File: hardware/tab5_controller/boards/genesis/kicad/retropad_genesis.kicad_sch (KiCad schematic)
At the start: 46 parts, among them J1 Tab5 Ext.Port1, J2 SWD, SW1 UP, SW10 START, SW11 MENU, SW12 L, SW13 R, SW2 DOWN, SW3 LEFT, SW4 RIGHT, SW5 X, SW6 B, SW7 Y, SW8 A, SW9 SELECT, U1 STM32F030C8T6

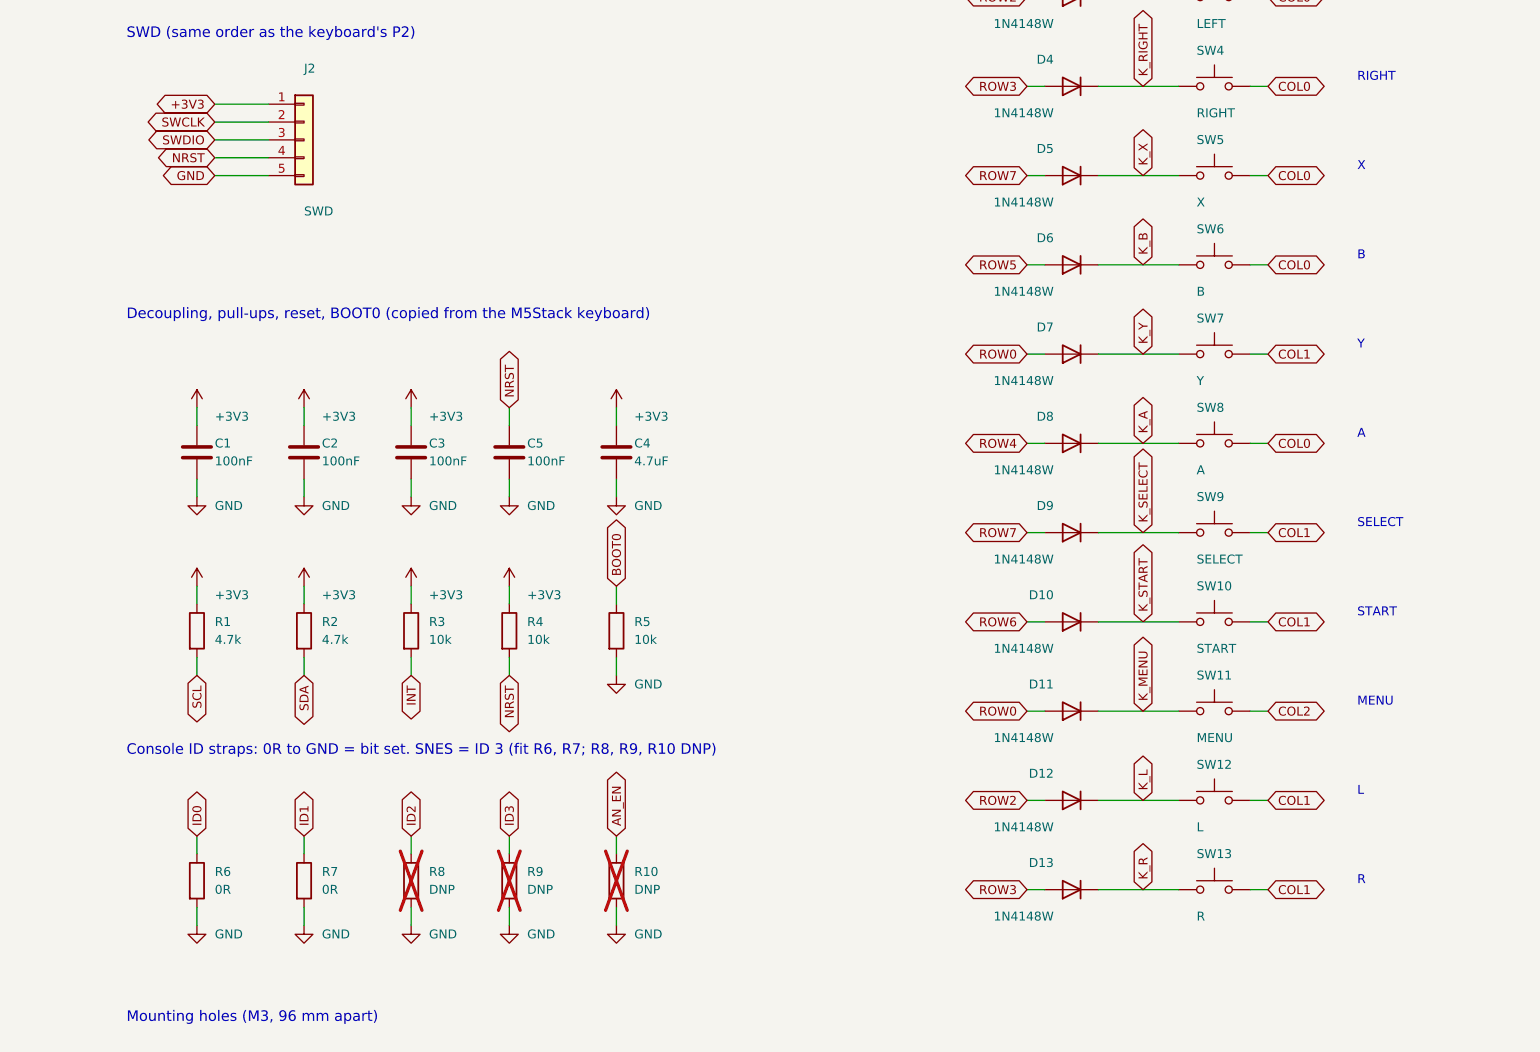
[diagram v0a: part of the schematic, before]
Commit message: tab5_controller: NES, Game Boy, Genesis and SMS/GG boards; shared generators
Generators move from boards/snes/kicad to boards/kicad_gen and take a
console name (gen_pcb.py, gen_sch.py, check_netlist.py, plus render.py);
console ids, titles and ID straps come from layout.CONSOLES.

New layouts in layout.py, each passing the clearance checks:
- NES (ID 1): B/A side by side, flat SELECT/START, MENU
- Game Boy (ID 2): diagonal B/A, flat SELECT/START (the angled pair left
  ROW7 unroutable), MENU
- Genesis (ID 5): A/B/C rising row, START, MENU
- Master System / Game Gear (ID 4): 1/2 on the B/A bits, START, MENU

All five boards are regenerated: routed with 0 unconnected pads and no
clearance/edge errors, schematic vs PCB 0 differences, ID straps and
button matrix wiring verified. Connector GND pins and SMD pads now join
the GND pour solidly, which removes starved-thermal errors.

Co-Authored-By: Claude Opus 5.5 <noreply@anthropic.com>
Claude-Session: https://claude.ai/code/session_01NhSHTsezreiVZCnuBhQzP2
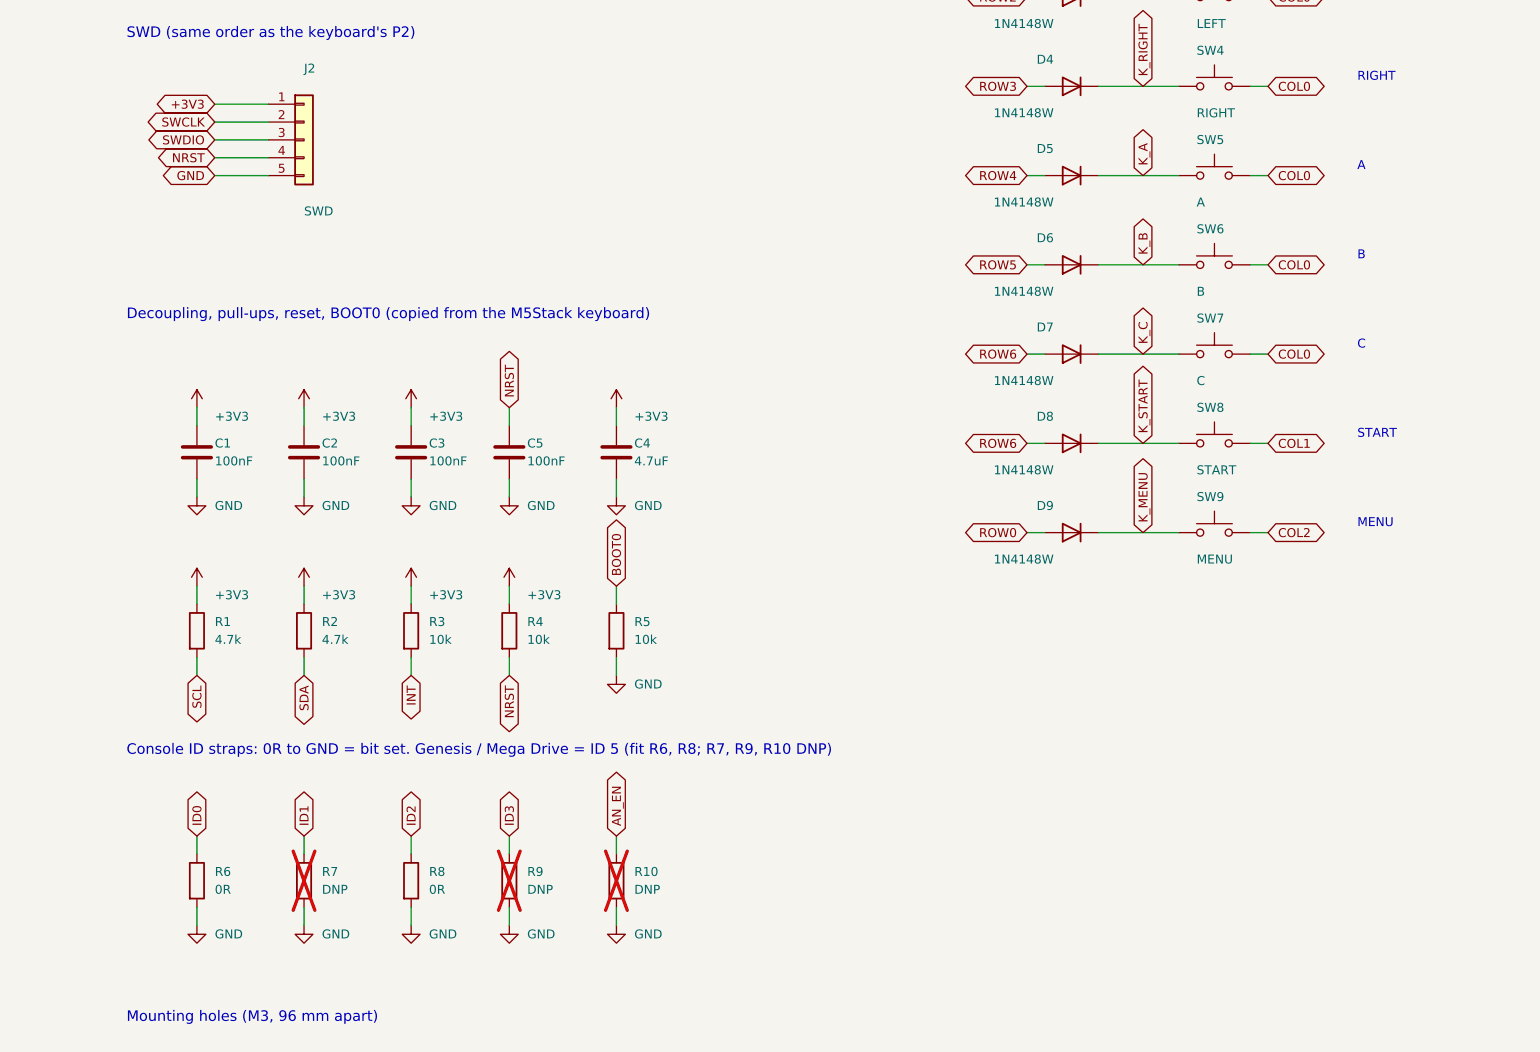
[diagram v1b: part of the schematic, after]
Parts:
- removed D10, D11, D12, D13: 1N4148W, Diode_SMD:D_SOD-123, symbol Device:D
- removed SW10: START, Button_Switch_THT:SW_PUSH_6mm, symbol Switch:SW_Push
- removed SW11: MENU, Button_Switch_THT:SW_PUSH_6mm, symbol Switch:SW_Push
- removed SW12: L, Button_Switch_THT:SW_Tactile_SPST_Angled_PTS645Vx31-2LFS, symbol Switch:SW_Push
- removed SW13: R, Button_Switch_THT:SW_Tactile_SPST_Angled_PTS645Vx31-2LFS, symbol Switch:SW_Push
- R7: value 0R -> DNP; now not fitted; now left out of the parts list
- R8: value DNP -> 0R; now fitted; now in the parts list
- SW5: value X -> A
- SW7: value Y -> C
- SW8: value A -> START; footprint Button_Switch_THT:SW_PUSH-12mm -> Button_Switch_THT:SW_PUSH_6mm
- SW9: value SELECT -> MENU
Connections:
- net K_SELECT is gone; now on net K_MENU: D9.1 (K), SW9.1
- net K_X is gone; now on net K_A: D5.1 (K), SW5.1
- net COL0: now also SW7.2; no longer SW8.2
- net COL1: now also SW8.2; no longer SW7.2, SW9.2
- net COL2: now also SW9.2
- net K_A: no longer D8.1 (K), SW8.1
- net K_START: now also D8.1 (K), SW8.1
- net ROW0: now also D9.2 (A); no longer D7.2 (A)
- net ROW4: now also D5.2 (A); no longer D8.2 (A)
- net ROW6: now also D7.2 (A), D8.2 (A)
- net ROW7: no longer D5.2 (A), D9.2 (A)
- net K_Y renamed K_C
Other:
- note added: "C"
- note added: "Console ID straps: 0R to GND = bit set. Genesis / Mega Drive = ID 5 (fit R6, R8; R7, R9, R10 DNP)"
- note removed: "Console ID straps: 0R to GND = bit set. SNES = ID 3 (fit R6, R7; R8, R9, R10 DNP)"
- note removed: "L"
- note removed: "R"
- note removed: "SELECT"
- note removed: "X"
- note removed: "Y"
- title: RetroPad SNES controller (console ID 3) -> RetroPad Genesis / Mega Drive controller (console ID 5)

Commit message: tab5_controller: redesign Genesis board as the 6-button pad
X Y Z now sit in a row above A B C (14 mm columns, rising 1.5 mm per
column, rows 16.5 mm apart), with MODE beside START on the SELECT bit and
MENU above. The board is re-routed: 0 unconnected pads, no DRC errors
beyond silkscreen warnings, schematic vs PCB 0 differences, and button
wiring and ID straps verified.

layout.py now also checks footprint courtyards and the M3 holes'
courtyards. The first 6-button attempt passed the pad checks but DRC
found overlapping courtyards; the four existing boards pass the new
check unchanged.

The Genesis core (gwenesis) still emulates only the 3-button pad, so
X/Y/Z/MODE are reported by the board but ignored until the core and the
host map gain 6-button support; documented in genesis/README.md.

Co-Authored-By: Claude Opus 5.5 <noreply@anthropic.com>
Claude-Session: https://claude.ai/code/session_01NhSHTsezreiVZCnuBhQzP2
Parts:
- added D10, D11, D12, D13: 1N4148W, Diode_SMD:D_SOD-123, symbol Device:D
- added SW10: Z, Button_Switch_THT:SW_PUSH-12mm, symbol Switch:SW_Push
- added SW11: MODE, Button_Switch_THT:SW_PUSH_6mm, symbol Switch:SW_Push
- added SW12: START, Button_Switch_THT:SW_PUSH_6mm, symbol Switch:SW_Push
- added SW13: MENU, Button_Switch_THT:SW_PUSH_6mm, symbol Switch:SW_Push
- SW6: value B -> X
- SW7: value C -> B
- SW8: value START -> Y; footprint Button_Switch_THT:SW_PUSH_6mm -> Button_Switch_THT:SW_PUSH-12mm
- SW9: value MENU -> C; footprint Button_Switch_THT:SW_PUSH_6mm -> Button_Switch_THT:SW_PUSH-12mm
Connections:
- net COL0: now also SW9.2
- net COL1: now also SW10.2, SW11.2, SW12.2
- net COL2: now also SW13.2; no longer SW9.2
- net K_B: now also D7.1 (K), SW7.1; no longer D6.1 (K), SW6.1
- net K_C: now also D9.1 (K), SW9.1; no longer D7.1 (K), SW7.1
- net K_MENU: now also D13.1 (K), SW13.1; no longer D9.1 (K), SW9.1
- net K_START: now also D12.1 (K), SW12.1; no longer D8.1 (K), SW8.1
- net ROW0: now also D8.2 (A), D13.2 (A); no longer D9.2 (A)
- net ROW1: now also D10.2 (A)
- net ROW5: now also D7.2 (A); no longer D6.2 (A)
- net ROW6: now also D9.2 (A), D12.2 (A); no longer D7.2 (A), D8.2 (A)
- net ROW7: now also D6.2 (A), D11.2 (A)
- new net K_MODE: D11.1 (K), SW11.1
- new net K_X: D6.1 (K), SW6.1
- new net K_Y: D8.1 (K), SW8.1
- new net K_Z: D10.1 (K), SW10.1
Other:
- note added: "Console ID straps: 0R to GND = bit set. Genesis / Mega Drive 6-button = ID 5 (fit R6, R8; R7, R9, R10 DNP)"
- note added: "MODE"
- note added: "X"
- note added: "Y"
- note added: "Z"
- note removed: "Console ID straps: 0R to GND = bit set. Genesis / Mega Drive = ID 5 (fit R6, R8; R7, R9, R10 DNP)"
- title: RetroPad Genesis / Mega Drive controller (console ID 5) -> RetroPad Genesis / Mega Drive 6-button controller (console ID 5)

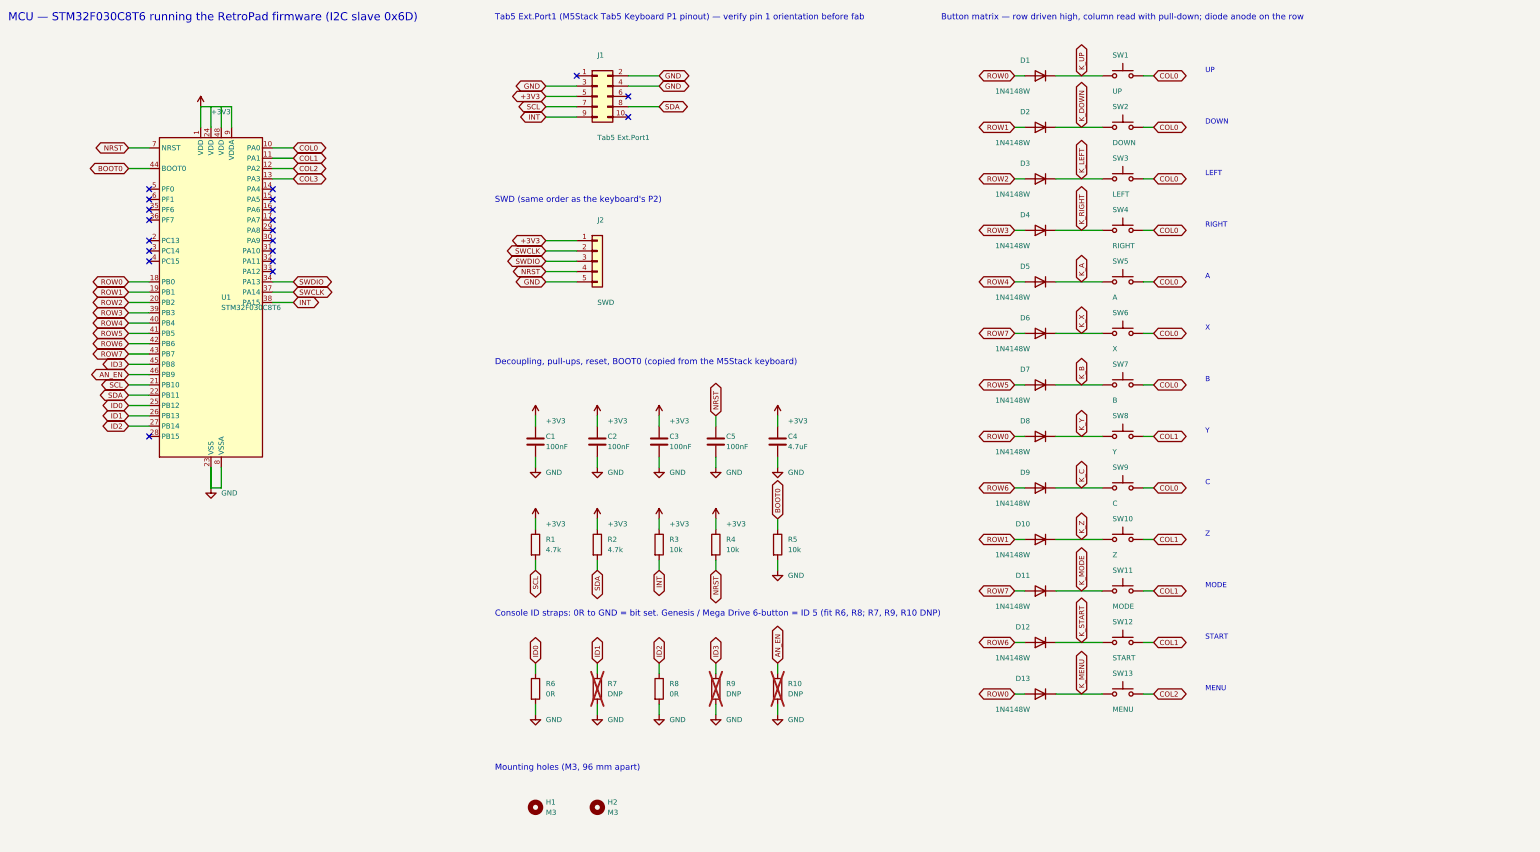
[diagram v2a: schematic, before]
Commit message: tab5_controller: build every console board on the AVR32DD28
The STM32F030 matrix boards are gone. SNES, NES, Game Boy, Genesis and
Master System / Game Gear are now all AVR32DD28 boards: one MCU pin per
button, no diodes, UPDI programming, one firmware image (firmware_avrdd)
keyed by the console-ID straps.

- layout.py / gen_pcb.py / gen_sch.py: drop the stm32 core (LQFP-48,
  key matrix, diodes, SWD header, AN_EN strap); the AVR DD core is the
  only one, and the *_dd board names become the plain console names.
- SNES, NES and Genesis keep the routing of their AVR DD prototypes;
  Game Boy and Master System are routed fresh.
- Every board: DRC 0 unconnected (silkscreen warnings only), schematic
  vs PCB 0 differences, and each switch checked against the MCU pin
  pinmap.h gives it for that console ID.
- Host test now also covers the Game Boy and Master System pin maps.
- READMEs describe the AVR DD boards only.

Co-Authored-By: Claude Opus 5.5 <noreply@anthropic.com>
Claude-Session: https://claude.ai/code/session_01NhSHTsezreiVZCnuBhQzP2
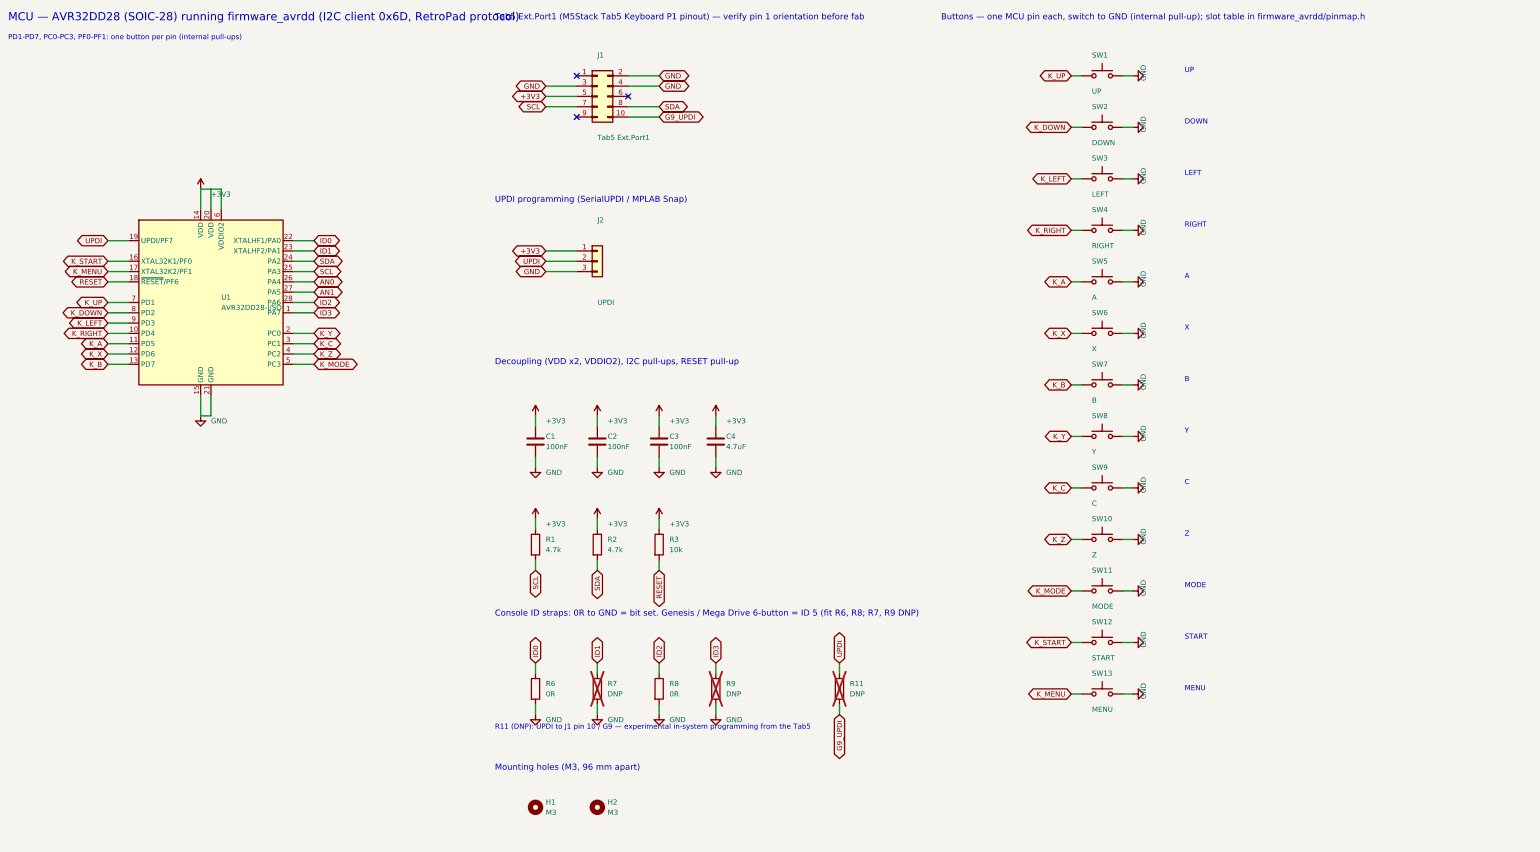
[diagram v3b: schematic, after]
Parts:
- removed C5: 100nF, Capacitor_SMD:C_0603_1608Metric, symbol Device:C
- removed D1, D10, D11, D12, D13, D2, D3, D4, D5, D6, D7, D8, D9: 1N4148W, Diode_SMD:D_SOD-123, symbol Device:D
- removed R10: DNP, Resistor_SMD:R_0603_1608Metric, symbol Device:R
- removed R4, R5: 10k, Resistor_SMD:R_0603_1608Metric, symbol Device:R
- added R11: DNP, Resistor_SMD:R_0603_1608Metric, symbol Device:R
- J2: value SWD -> UPDI; footprint Connector_PinHeader_2.54mm:PinHeader_1x05_P2.54mm_Vertical -> Connector_PinHeader_2.54mm:PinHeader_1x03_P2.54mm_Vertical; symbol Connector_Generic:Conn_01x05 -> Connector_Generic:Conn_01x03
- U1: value STM32F030C8T6 -> AVR32DD28-I/SO; footprint Package_QFP:LQFP-48_7x7mm_P0.5mm -> Package_SO:SOIC-28W_7.5x17.9mm_P1.27mm; symbol MCU_ST_STM32F0:STM32F030C8Tx -> RetroPad:AVR32DD28-xSO
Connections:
- net COL3 is gone; now on net K_B: U1.13 (PD7)
- net ROW2 is gone; now on net +3V3: U1.20 (VDD)
- net +3V3: now also U1.14 (VDD), U1.6 (VDDIO2); no longer U1.1 (VDD), U1.24 (VDD), U1.48 (VDD), U1.9 (VDDA)
- net GND: now also J2.3 (Pin_3), SW1.2, SW10.2, SW11.2, SW12.2, SW13.2, SW2.2, SW3.2, SW4.2, SW5.2, SW6.2, SW7.2, SW8.2, SW9.2, U1.15 (GND), U1.21 (GND); no longer J2.5 (Pin_5), U1.23 (VSS), U1.47 (VSS), U1.8 (VSSA)
- net ID0: now also U1.22 (XTALHF1/PA0); no longer U1.25 (PB12)
- net ID1: now also U1.23 (XTALHF2/PA1); no longer U1.26 (PB13)
- net ID2: now also U1.28 (PA6); no longer U1.27 (PB14)
- net ID3: now also U1.1 (PA7); no longer U1.45 (PB8)
- net K_A: now also U1.11 (PD5)
- net K_C: now also U1.3 (PC1)
- net K_DOWN: now also U1.8 (PD2)
- net K_LEFT: now also U1.9 (PD3)
- net K_MENU: now also U1.17 (XTAL32K2/PF1)
- net K_MODE: now also U1.5 (PC3)
- net K_RIGHT: now also U1.10 (PD4)
- net K_START: now also U1.16 (XTAL32K1/PF0)
- net K_UP: now also U1.7 (PD1)
- net K_X: now also U1.12 (PD6)
- net K_Y: now also U1.2 (PC0)
- net K_Z: now also U1.4 (PC2)
- net SCL: now also U1.25 (PA3); no longer U1.21 (PB10)
- net SDA: now also U1.24 (PA2); no longer U1.22 (PB11)
- net G9_UPDI: now reaches J1.10 (Pin_10)
- net G9_UPDI: now also R11.2
- removed net AN_EN: U1.46 (PB9)
- removed net BOOT0: U1.44 (BOOT0)
- removed net COL0: SW1.2, SW2.2, SW3.2, SW4.2, SW5.2, SW6.2, SW7.2, SW9.2, U1.10 (PA0)
- removed net COL1: SW10.2, SW11.2, SW12.2, SW8.2, U1.11 (PA1)
- removed net COL2: SW13.2, U1.12 (PA2)
- removed net INT: J1.9 (Pin_9), R3.2, U1.38 (PA15)
- removed net NRST: J2.4 (Pin_4), U1.7 (NRST)
- net ROW0 renamed RESET
- net RESET: now also R3.2
- net ROW1 renamed UPDI
- net UPDI: now also J2.2 (Pin_2), R11.1
- removed net ROW3: U1.39 (PB3)
- removed net ROW4: U1.40 (PB4)
- removed net ROW5: U1.41 (PB5)
- removed net ROW6: U1.42 (PB6)
- removed net ROW7: U1.43 (PB7)
- removed net SWCLK: J2.2 (Pin_2), U1.37 (PA14)
- removed net SWDIO: J2.3 (Pin_3), U1.34 (PA13)
- new net AN0: U1.26 (PA4)
- new net AN1: U1.27 (PA5)
- no-connect marks 20 -> 3
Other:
- note added: "Buttons — one MCU pin each, switch to GND (internal pull-up); slot table in firmware_avrdd/pinmap.h"
- note added: "Console ID straps: 0R to GND = bit set. Genesis / Mega Drive 6-button = ID 5 (fit R6, R8; R7, R9 DNP)"
- note added: "Decoupling (VDD x2, VDDIO2), I2C pull-ups, RESET pull-up"
- note added: "MCU — AVR32DD28 (SOIC-28) running firmware_avrdd (I2C client 0x6D, RetroPad protocol)"
- note added: "PD1-PD7, PC0-PC3, PF0-PF1: one button per pin (internal pull-ups)"
- note added: "R11 (DNP): UPDI to J1 pin 10 / G9 — experimental in-system programming from the Tab5"
- note added: "UPDI programming (SerialUPDI / MPLAB Snap)"
- note removed: "Button matrix — row driven high, column read with pull-down; diode anode on the row"
- note removed: "Console ID straps: 0R to GND = bit set. Genesis / Mega Drive 6-button = ID 5 (fit R6, R8; R7, R9, R10 DNP)"
- note removed: "Decoupling, pull-ups, reset, BOOT0 (copied from the M5Stack keyboard)"
- note removed: "MCU — STM32F030C8T6 running the RetroPad firmware (I2C slave 0x6D)"
- note removed: "SWD (same order as the keyboard's P2)"
- moved on the sheet: C4, SW1, SW10, SW11, SW12, SW13, SW2, SW3, SW4, SW5, SW6, SW7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
